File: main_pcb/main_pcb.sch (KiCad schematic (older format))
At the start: 54 parts, among them J1 DBG, J2 UI, J3 UI, J4 Raspberry_Pi_Zero_WH, J5 UI, J6 UI, J7 UPDN, J8 ISP, J9 BTN_TRIG, Q1 BSS123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

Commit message: Updated main pcb BOM
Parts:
- BT1, H1, H2, H3, H4: MPN (none) -> DNP; Manufacturer (none) -> DNP
- Q1: Manufacturer ON Semiconductor -> Changjiang Electronics Tech (CJ)
- Q2: value HSS2307 -> WTM2300; MPN HSS2307 -> WTM2300; Manufacturer Huashuo -> WPMtek(Wei Pan Microelectronics)
- R5: MPN (none) -> RC0603FR-07100KL; Manufacturer (none) -> YAGEO
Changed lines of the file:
@@
 F 2 "MountingHole:MountingHole_3.2mm_M3_Pad" H 6100 6600 50  0001 C CNN
 F 3 "~" H 6100 6600 50  0001 C CNN
+F 4 "DNP" H 6100 6600 50  0001 C CNN "MPN"
+F 5 "DNP" H 6100 6600 50  0001 C CNN "Manufacturer"
 	1    6100 6600
 	1    0    0    -1
@@
 F 2 "MountingHole:MountingHole_3.2mm_M3_Pad" H 6100 6900 50  0001 C CNN
 F 3 "~" H 6100 6900 50  0001 C CNN
+F 4 "DNP" H 6100 6900 50  0001 C CNN "MPN"
+F 5 "DNP" H 6100 6900 50  0001 C CNN "Manufacturer"
 	1    6100 6900
 	1    0    0    -1
@@
 F 2 "MountingHole:MountingHole_3.2mm_M3_Pad" H 6100 7200 50  0001 C CNN
 F 3 "~" H 6100 7200 50  0001 C CNN
+F 4 "DNP" H 6100 7200 50  0001 C CNN "MPN"
+F 5 "DNP" H 6100 7200 50  0001 C CNN "Manufacturer"
 	1    6100 7200
 	1    0    0    -1
@@
 F 2 "MountingHole:MountingHole_3.2mm_M3_Pad" H 6100 7500 50  0001 C CNN
 F 3 "~" H 6100 7500 50  0001 C CNN
+F 4 "DNP" H 6100 7500 50  0001 C CNN "MPN"
+F 5 "DNP" H 6100 7500 50  0001 C CNN "Manufacturer"
 	1    6100 7500
 	1    0    0    -1
@@
 P 2250 1050
 F 0 "Q2" V 2592 1050 50  0000 C CNN
-F 1 "HSS2307" V 2501 1050 50  0000 C CNN
+F 1 "WTM2300" V 2501 1050 50  0000 C CNN
 F 2 "Package_TO_SOT_SMD:SOT-23W" H 2450 1150 50  0001 C CNN
 F 3 "~" H 2250 1050 50  0001 C CNN
-F 4 "HSS2307" H 2250 1050 50  0001 C CNN "MPN"
-F 5 "Huashuo" H 2250 1050 50  0001 C CNN "Manufacturer"
+F 4 "WTM2300" H 2250 1050 50  0001 C CNN "MPN"
+F 5 "WPMtek(Wei Pan Microelectronics)" H 2250 1050 50  0001 C CNN "Manufacturer"
 	1    2250 1050
 	0    1    -1   0
@@
 F 2 "Connector_PinHeader_2.54mm:PinHeader_2x01_P2.54mm_Vertical" V 650 1410 50  0001 C CNN
 F 3 "~" V 650 1410 50  0001 C CNN
+F 4 "DNP" H 650 1350 50  0001 C CNN "Manufacturer"
+F 5 "DNP" H 650 1350 50  0001 C CNN "MPN"
 	1    650  1350
 	1    0    0    -1
@@
 F 2 "Package_TO_SOT_SMD:SOT-23" H 2550 1475 50  0001 L CIN
 F 3 "http://www.diodes.com/assets/Datasheets/ds30366.pdf" H 2350 1550 50  0001 L CNN
-F 4 "ON Semiconductor" H 2350 1550 50  0001 C CNN "Manufacturer"
+F 4 "Changjiang Electronics Tech (CJ)" H 2350 1550 50  0001 C CNN "Manufacturer"
 F 5 "BSS123" H 2350 1550 50  0001 C CNN "MPN"
 	1    2350 1550
@@
 F 2 "Resistor_SMD:R_0603_1608Metric" V 9280 3800 50  0001 C CNN
 F 3 "~" H 9350 3800 50  0001 C CNN
+F 4 "YAGEO" H 9350 3800 50  0001 C CNN "Manufacturer"
+F 5 "RC0603FR-07100KL" H 9350 3800 50  0001 C CNN "MPN"
 	1    9350 3800
 	0    1    1    0

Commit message: Fixed two MPN
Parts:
- J8: MPN C9135 -> C11214
- SW1: MPN TS4570CJ -> K2-1102DP-J4SW-04; Manufacturer SHOU HAN -> Korean Hroparts Elec
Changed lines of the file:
@@
 F 3 "~" H 10400 6100 50  0001 C CNN
 F 4 "BOOMELE" H 10400 6100 50  0001 C CNN "Manufacturer"
-F 5 "C9135" H 10400 6100 50  0001 C CNN "MPN"
+F 5 "C11214" H 10400 6100 50  0001 C CNN "MPN"
 	1    10400 6100
 	1    0    0    -1
@@
 F 2 "Button_Switch_THT:SW_PUSH_6mm_H8mm" H 1500 1850 50  0001 C CNN
 F 3 "~" H 1500 1850 50  0001 C CNN
-F 4 "TS4570CJ" H 1500 1850 50  0001 C CNN "MPN"
-F 5 "SHOU HAN" H 1500 1850 50  0001 C CNN "Manufacturer"
+F 4 "K2-1102DP-J4SW-04" H 1500 1850 50  0001 C CNN "MPN"
+F 5 "Korean Hroparts Elec" H 1500 1850 50  0001 C CNN "Manufacturer"
 	1    1500 1850
 	1    0    0    -1

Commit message: Fixed wrong pinout of p-channel mosfet for power control on main pcb and module pcb
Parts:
- removed Q2: WTM2300, Package_TO_SOT_SMD:SOT-23W, symbol Device:Q_PMOS_SGD
- added Q2: WTM2300, Package_TO_SOT_SMD:SOT-23W, symbol Device:Q_PMOS_GSD
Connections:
- net +BATT: now also Q2.3 (D)
- net BAT_RAW: now also Q2.2 (S)
- net at D2.2 (A), Q1.3 (D), R6.2: now also Q2.1 (G)
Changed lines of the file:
@@
 	1    0    0    -1
-$EndComp
-$Comp
-L Device:Q_PMOS_SGD Q2
-U 1 1 61CC827D
-P 2250 1050
-F 0 "Q2" V 2592 1050 50  0000 C CNN
-F 1 "WTM2300" V 2501 1050 50  0000 C CNN
-F 2 "Package_TO_SOT_SMD:SOT-23W" H 2450 1150 50  0001 C CNN
-F 3 "~" H 2250 1050 50  0001 C CNN
-F 4 "WTM2300" H 2250 1050 50  0001 C CNN "MPN"
-F 5 "WPMtek(Wei Pan Microelectronics)" H 2250 1050 50  0001 C CNN "Manufacturer"
-	1    2250 1050
-	0    1    -1   0
 $EndComp
 Wire Wire Line
@@
 Wire Wire Line
 	9200 3800 8900 3800
+$Comp
+L Device:Q_PMOS_GSD Q2
+U 1 1 61930F7D
+P 2250 1050
+F 0 "Q2" V 2592 1050 50  0000 C CNN
+F 1 "WTM2300" V 2501 1050 50  0000 C CNN
+F 2 "Package_TO_SOT_SMD:SOT-23W" H 2450 1150 50  0001 C CNN
+F 3 "~" H 2250 1050 50  0001 C CNN
+F 4 "WPMtek(Wei Pan Microelectronics)" H 2250 1050 50  0001 C CNN "Manufacturer"
+F 5 "WTM2300" H 2250 1050 50  0001 C CNN "MPN"
+	1    2250 1050
+	0    1    -1   0
+$EndComp
 $EndSCHEMATC

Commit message: Fixed part number of n-channel power mosfet (the selected one was an n-channel)
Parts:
- Q2: value WTM2300 -> HSS2307; MPN WTM2300 -> HSS2307; Manufacturer WPMtek(Wei Pan Microelectronics) -> Huashuo
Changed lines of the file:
@@
 P 2250 1050
 F 0 "Q2" V 2592 1050 50  0000 C CNN
-F 1 "WTM2300" V 2501 1050 50  0000 C CNN
+F 1 "HSS2307" V 2501 1050 50  0000 C CNN
 F 2 "Package_TO_SOT_SMD:SOT-23W" H 2450 1150 50  0001 C CNN
 F 3 "~" H 2250 1050 50  0001 C CNN
-F 4 "WPMtek(Wei Pan Microelectronics)" H 2250 1050 50  0001 C CNN "Manufacturer"
-F 5 "WTM2300" H 2250 1050 50  0001 C CNN "MPN"
+F 4 "Huashuo" H 2250 1050 50  0001 C CNN "Manufacturer"
+F 5 "HSS2307" H 2250 1050 50  0001 C CNN "MPN"
 	1    2250 1050
 	0    1    -1   0

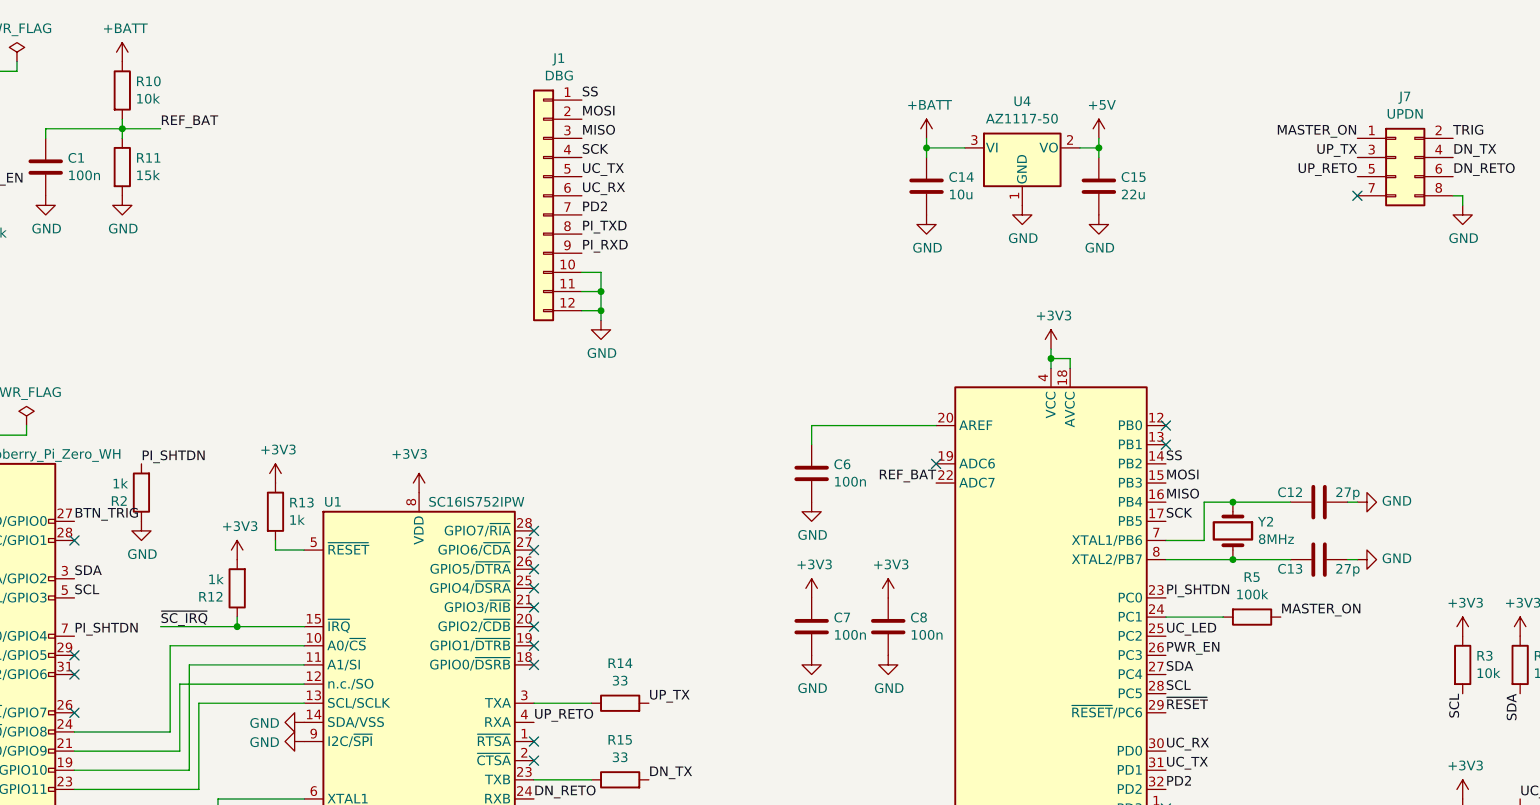
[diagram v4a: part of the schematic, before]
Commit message: Modified resistor divider for power measurement, replaced resistor with diode for master button input
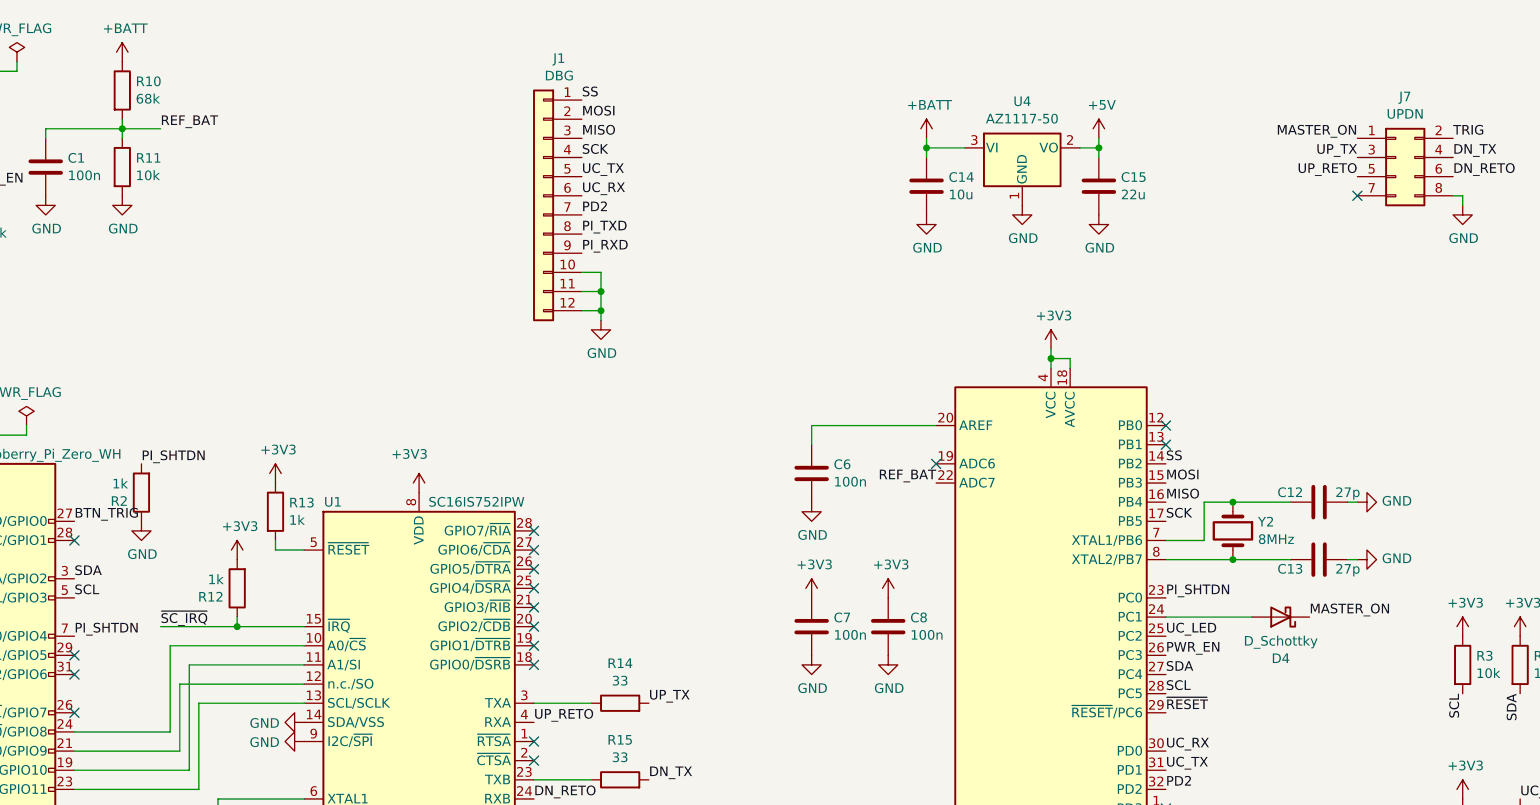
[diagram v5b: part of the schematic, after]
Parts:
- removed R5: 100k, Resistor_SMD:R_0603_1608Metric, symbol Device:R
- added D4: D_Schottky, Diode_SMD:D_SOD-123, symbol Device:D_Schottky
- R10: value 10k -> 68k; MPN RC0603JR-0710KL -> RC0603JR-0768KL
- R11: value 15k -> 10k; MPN RC0603JR-0715KL -> RC0603JR-0710KL
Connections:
- net MASTER_ON: now also D4.1 (K)
- net at U3.24 (PC1): now also D4.2 (A)
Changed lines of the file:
@@
 P 3450 1050
 F 0 "R10" H 3520 1096 50  0000 L CNN
-F 1 "10k" H 3520 1005 50  0000 L CNN
+F 1 "68k" H 3520 1005 50  0000 L CNN
 F 2 "Resistor_SMD:R_0603_1608Metric" V 3380 1050 50  0001 C CNN
 F 3 "~" H 3450 1050 50  0001 C CNN
 F 4 "YAGEO" H 3450 1050 50  0001 C CNN "Manufacturer"
-F 5 "RC0603JR-0710KL" H 3450 1050 50  0001 C CNN "MPN"
+F 5 "RC0603JR-0768KL" H 3450 1050 50  0001 C CNN "MPN"
 	1    3450 1050
 	1    0    0    -1
@@
 P 3450 1450
 F 0 "R11" H 3520 1496 50  0000 L CNN
-F 1 "15k" H 3520 1405 50  0000 L CNN
+F 1 "10k" H 3520 1405 50  0000 L CNN
 F 2 "Resistor_SMD:R_0603_1608Metric" V 3380 1450 50  0001 C CNN
 F 3 "~" H 3450 1450 50  0001 C CNN
 F 4 "YAGEO" H 3450 1450 50  0001 C CNN "Manufacturer"
-F 5 "RC0603JR-0715KL" H 3450 1450 50  0001 C CNN "MPN"
+F 5 "RC0603JR-0710KL" H 3450 1450 50  0001 C CNN "MPN"
 	1    3450 1450
 	1    0    0    -1
@@
 	5350 6850 5350 6900
 NoConn ~ 1600 3700
-Text Label 9500 3800 0    50   ~ 0
+Text Label 9650 3800 0    50   ~ 0
 MASTER_ON
-$Comp
-L Device:R R5
-U 1 1 61854BF3
-P 9350 3800
-F 0 "R5" V 9143 3800 50  0000 C CNN
-F 1 "100k" V 9234 3800 50  0000 C CNN
-F 2 "Resistor_SMD:R_0603_1608Metric" V 9280 3800 50  0001 C CNN
-F 3 "~" H 9350 3800 50  0001 C CNN
-F 4 "YAGEO" H 9350 3800 50  0001 C CNN "Manufacturer"
-F 5 "RC0603FR-07100KL" H 9350 3800 50  0001 C CNN "MPN"
-	1    9350 3800
-	0    1    1    0
-$EndComp
-Wire Wire Line
-	9200 3800 8900 3800
+Wire Wire Line
+	9350 3800 8900 3800
 $Comp
 L Device:Q_PMOS_GSD Q2
@@
 	0    1    -1   0
 $EndComp
+$Comp
+L Device:D_Schottky D4
+U 1 1 61A2784D
+P 9500 3800
+F 0 "D4" H 9500 4017 50  0000 C CNN
+F 1 "D_Schottky" H 9500 3926 50  0000 C CNN
+F 2 "Diode_SMD:D_SOD-123" H 9500 3800 50  0001 C CNN
+F 3 "~" H 9500 3800 50  0001 C CNN
+F 4 "Guangdong Hottech" H 9500 3800 50  0001 C CNN "Manufacturer"
+F 5 "SD103AW" H 9500 3800 50  0001 C CNN "MPN"
+	1    9500 3800
+	-1   0    0    1
+$EndComp
 $EndSCHEMATC

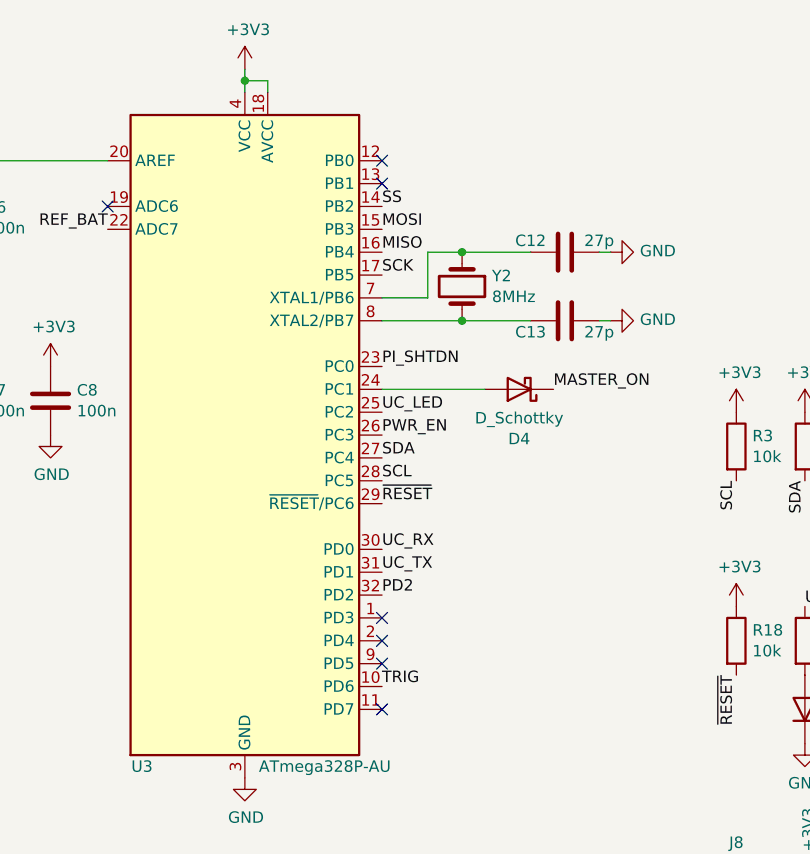
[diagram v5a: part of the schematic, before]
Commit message: Moved TRIG wire on a different pin to use timer1 instead of timer0 to have a 16 bit timer, which is also already implemented in the firmware
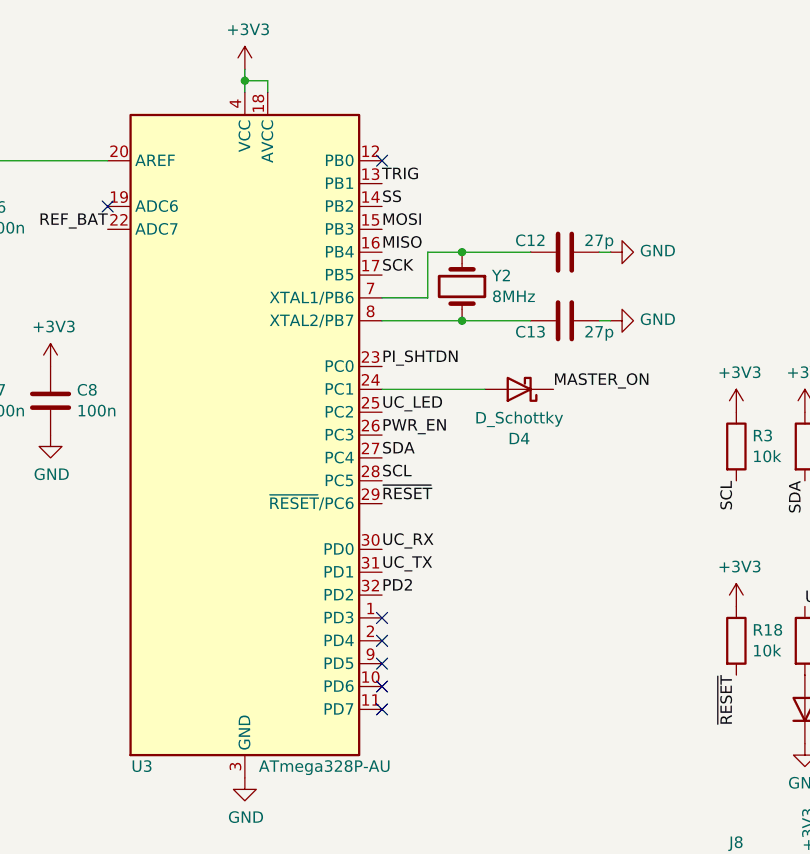
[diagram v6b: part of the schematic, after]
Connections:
- net TRIG: now also U3.13 (PB1); no longer U3.10 (PD6)
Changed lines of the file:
@@
 Text Label 5850 1700 0    50   ~ 0
 PD2
-Text Label 8900 5100 0    50   ~ 0
+Text Label 8900 2900 0    50   ~ 0
 TRIG
 Text Label 8900 4000 0    50   ~ 0
@@
 Connection ~ 2550 950
 NoConn ~ 8900 2800
-NoConn ~ 8900 2900
 NoConn ~ 7700 3000
 Text Label 5300 6750 0    50   ~ 0
@@
 	-1   0    0    1
 $EndComp
+NoConn ~ 8900 5100
 $EndSCHEMATC
